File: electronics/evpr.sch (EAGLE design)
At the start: 140 parts

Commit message: Negative using signals correctly marked as negative
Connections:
- net USING_ENG renamed !USING_ENG
- new net !USING_BAT: U.ESP1.IO4
- net USING_BAT: no longer U.ESP1.IO4
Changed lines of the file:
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@@
 </segment>
 </net>
-<net name="USING_ENG" class="0">
+<net name="!USING_ENG" class="0">
 <segment>
 <pinref part="U.YY1" gate="A" pin="!ONST2"/>
@@
 <wire x1="-38.1" y1="-15.24" x2="-38.1" y2="-30.48" width="0.1524" layer="91"/>
 <wire x1="-38.1" y1="-30.48" x2="-35.56" y2="-30.48" width="0.1524" layer="91"/>
-</segment>
-<segment>
-<label x="114.3" y="152.4" size="1.778" layer="95" xref="yes"/>
-<pinref part="U.ESP1" gate="G$1" pin="IO4"/>
-<wire x1="73.66" y1="139.7" x2="96.52" y2="139.7" width="0.1524" layer="91"/>
-<wire x1="96.52" y1="139.7" x2="96.52" y2="152.4" width="0.1524" layer="91"/>
-<wire x1="96.52" y1="152.4" x2="114.3" y2="152.4" width="0.1524" layer="91"/>
 </segment>
 </net>
@@
 </segment>
 </net>
+<net name="!USING_BAT" class="0">
+<segment>
+<label x="114.3" y="152.4" size="1.778" layer="95" xref="yes"/>
+<pinref part="U.ESP1" gate="G$1" pin="IO4"/>
+<wire x1="73.66" y1="139.7" x2="96.52" y2="139.7" width="0.1524" layer="91"/>
+<wire x1="96.52" y1="139.7" x2="96.52" y2="152.4" width="0.1524" layer="91"/>
+<wire x1="96.52" y1="152.4" x2="114.3" y2="152.4" width="0.1524" layer="91"/>
+</segment>
+</net>

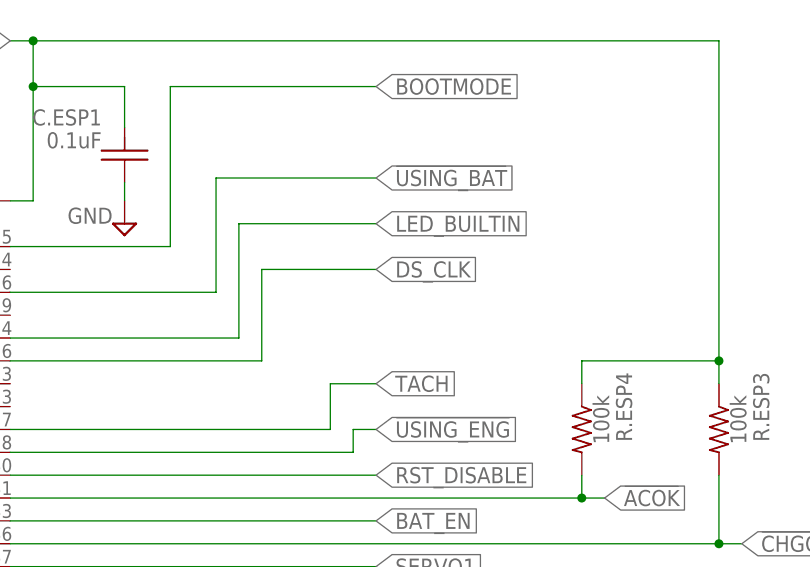
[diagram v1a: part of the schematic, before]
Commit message: Unswap DS_CLK and LED_Builtin
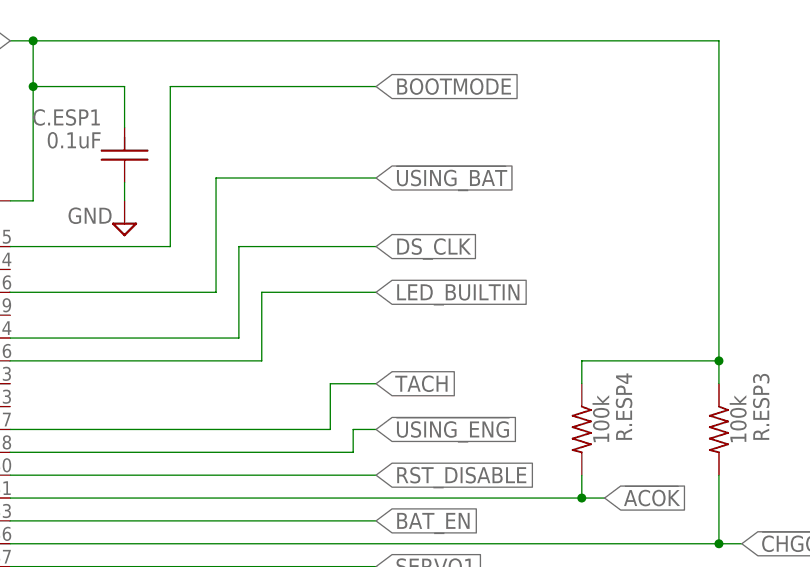
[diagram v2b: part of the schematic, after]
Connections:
- net DS_CLK: now also U.ESP1.IO12; no longer U.ESP1.IO13
- net LED_BUILTIN: now also U.ESP1.IO13; no longer U.ESP1.IO12
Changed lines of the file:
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@@
 </segment>
 <segment>
-<label x="114.3" y="142.24" size="1.778" layer="95" xref="yes"/>
-<wire x1="101.6" y1="142.24" x2="114.3" y2="142.24" width="0.1524" layer="91"/>
-<pinref part="U.ESP1" gate="G$1" pin="IO13"/>
-<wire x1="73.66" y1="132.08" x2="101.6" y2="132.08" width="0.1524" layer="91"/>
-<wire x1="101.6" y1="132.08" x2="101.6" y2="142.24" width="0.1524" layer="91"/>
+<label x="114.3" y="144.78" size="1.778" layer="95" xref="yes"/>
+<wire x1="99.06" y1="144.78" x2="114.3" y2="144.78" width="0.1524" layer="91"/>
+<pinref part="U.ESP1" gate="G$1" pin="IO12"/>
+<wire x1="99.06" y1="134.62" x2="99.06" y2="144.78" width="0.1524" layer="91"/>
+<wire x1="73.66" y1="134.62" x2="99.06" y2="134.62" width="0.1524" layer="91"/>
 </segment>
 </net>
@@
 <net name="LED_BUILTIN" class="0">
 <segment>
-<pinref part="U.ESP1" gate="G$1" pin="IO12"/>
-<wire x1="73.66" y1="134.62" x2="99.06" y2="134.62" width="0.1524" layer="91"/>
-<wire x1="99.06" y1="134.62" x2="99.06" y2="147.32" width="0.1524" layer="91"/>
-<wire x1="99.06" y1="147.32" x2="114.3" y2="147.32" width="0.1524" layer="91"/>
-<label x="114.3" y="147.32" size="1.778" layer="95" xref="yes"/>
-</segment>
-<segment>
+<wire x1="101.6" y1="132.08" x2="101.6" y2="139.7" width="0.1524" layer="91"/>
+<wire x1="101.6" y1="139.7" x2="114.3" y2="139.7" width="0.1524" layer="91"/>
+<label x="114.3" y="139.7" size="1.778" layer="95" xref="yes"/>
+<pinref part="U.ESP1" gate="G$1" pin="IO13"/>
+<wire x1="73.66" y1="132.08" x2="101.6" y2="132.08" width="0.1524" layer="91"/>
+</segment>
+<segment>

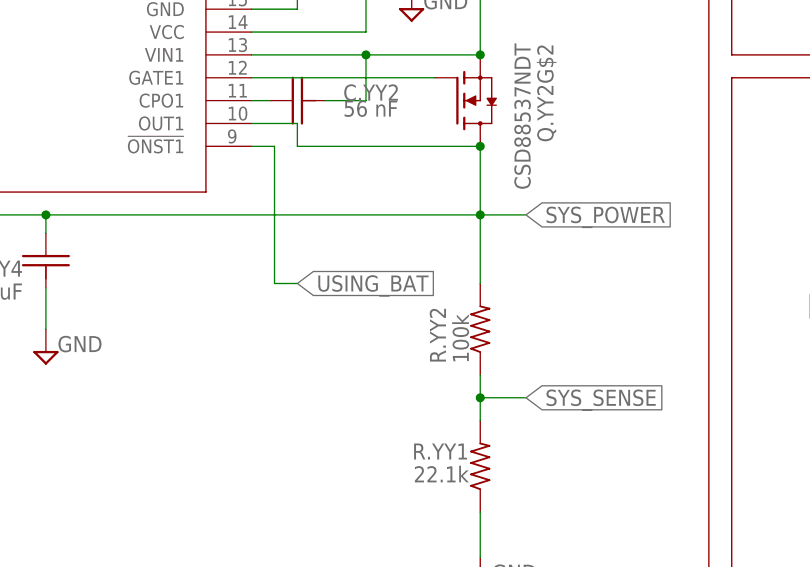
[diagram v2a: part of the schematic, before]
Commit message: Performed DRC checks, fixed minor issues, redid OSH version
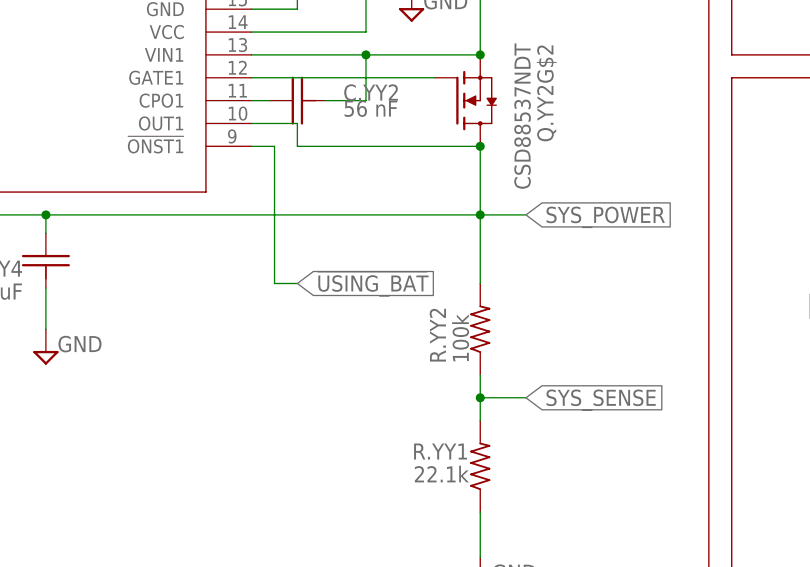
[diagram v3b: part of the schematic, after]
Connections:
- removed net USING_BAT: U.YY1.!ONST1
- net !USING_BAT: now also U.YY1.!ONST1
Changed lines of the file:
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@@
-</segment>
-</net>
-<net name="USING_BAT" class="0">
-<segment>
-<pinref part="U.YY1" gate="A" pin="!ONST1"/>
-<label x="-35.56" y="-30.48" size="1.778" layer="95" rot="MR180" xref="yes"/>
-<wire x1="-40.64" y1="-15.24" x2="-38.1" y2="-15.24" width="0.1524" layer="91"/>
-<wire x1="-38.1" y1="-15.24" x2="-38.1" y2="-30.48" width="0.1524" layer="91"/>
-<wire x1="-38.1" y1="-30.48" x2="-35.56" y2="-30.48" width="0.1524" layer="91"/>
 </segment>
 </net>
@@
 <wire x1="96.52" y1="152.4" x2="114.3" y2="152.4" width="0.1524" layer="91"/>
 </segment>
+<segment>
+<pinref part="U.YY1" gate="A" pin="!ONST1"/>
+<label x="-35.56" y="-30.48" size="1.778" layer="95" rot="MR180" xref="yes"/>
+<wire x1="-40.64" y1="-15.24" x2="-38.1" y2="-15.24" width="0.1524" layer="91"/>
+<wire x1="-38.1" y1="-15.24" x2="-38.1" y2="-30.48" width="0.1524" layer="91"/>
+<wire x1="-38.1" y1="-30.48" x2="-35.56" y2="-30.48" width="0.1524" layer="91"/>
+</segment>
 </net>
 </nets>
 </sheet>
 </sheets>
+<errors>
+</errors>
 </schematic>
 </drawing>

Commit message: Remove USB interface from EVPR, design external programmer board
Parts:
- removed C.USB1, C.USB4: 4.7uF, mccloud:C0603
- removed C.USB2, C.USB3: 0.1uF, mccloud:C0603
- removed C.USB5: 4.7 nF, mccloud:C0603
- removed Q.ESP1: DMN5L06K-7, mccloud:DMN5L06K-7
- removed Q.USB1, Q.USB2: MMBT2222A, transistor-neu-to92:MMBT2222ALT1-NPN-SOT23-BEC
- removed R.ESP1, R.USB2, R.USB3: 10k, mccloud:R0603
- removed R.USB1: 1k, mccloud:R0603
- removed R.USB5: 22.1k, mccloud:R0603
- removed R.USB6: 47.5K, mccloud:R0603
- removed R.USB7: 1M, mccloud:R0603
- removed SJ.ESP1: (no value), jumper:SJ
- removed TP11, TP14, TP15, TP3, TP5, TP7, TP8: PTR1TP10R, testpad:PTR1TP10R
- removed U.USB1: CP2102N-A02-GQFN24R, mccloud:CP2102N-A02-GQFN24R
- removed X.ESP2: RSTBTN, mccloud:RSTBTN
- removed X.USB1: 10118193-0001LF, mccloud:10118193-0001LF
- added SV1: (no value), con-lstb:MA04-2
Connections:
- removed net N$1: Q.ESP1.D, X.ESP2.1
- removed net N$16: R.USB1.1, U.USB1.RSTB
- removed net N$18: Q.USB1.E, R.USB3.2, TP14.TP, U.USB1.RTS
- removed net N$19: Q.USB2.E, R.USB2.2, TP8.TP, U.USB1.DTR
- removed net N$20: Q.USB1.B, R.USB2.1
- removed net N$21: Q.USB2.B, R.USB3.1
- removed net N$34: C.USB5.2, R.USB7.2, TP15.TP, X.USB1.SHIELD
- removed net N$39: R.USB1.2, U.USB1.VIO
- removed net N$40: C.USB1.2, C.USB2.2, TP3.TP, U.USB1.VDD
- removed net RST_DISABLE: Q.ESP1.G, R.ESP1.2, U.ESP1.IO18
- removed net USBD+: U.USB1.D+, X.USB1.D+
- removed net USBD-: U.USB1.D-, X.USB1.D-
- removed net USBSENSE: R.USB5.1, R.USB6.2, U.ESP1.IO20, U.USB1.VBUS
- removed net VUSB: C.USB3.2, C.USB4.2, Q.DS1.A, Q.ZZ2.A, R.USB5.2, TP7.TP, U.USB1.VREGIN, X.USB1.VUSB
- new net VPROG: Q.DS1.A, Q.ZZ2.A, SV1.6
- net BOOTMODE: now also SV1.3; no longer Q.USB2.C, TP11.TP
- net ESP_POWER: now also SV1.8; no longer R.ESP1.1
- net ESP_RX: now also SV1.5; no longer U.USB1.TXD
- net ESP_TX: now also SV1.7; no longer U.USB1.RXD
- net GND: now also SV1.2; no longer C.USB1.1, C.USB2.1, C.USB3.1, C.USB4.1, C.USB5.1, Q.ESP1.S, R.USB6.1, R.USB7.1, SJ.ESP1.1, U.USB1.GND, X.USB1.GND
- net RESET: now also SV1.1; no longer Q.USB1.C, SJ.ESP1.2, TP5.TP, X.ESP2.2
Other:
- note added: "ESP: ESP32 GPIO & Prog Interface"
- note removed: "ESP: ESP32 GPIO & Reset"
- note removed: "NOTE: LED_BUILTIN will blink during flashing. This is why the LED circuit is included here, rather than in the ESP32 block."
- note removed: "USB: USB Interface"
- moved on the sheet: D.USB1, R.ESP2, R.USB4

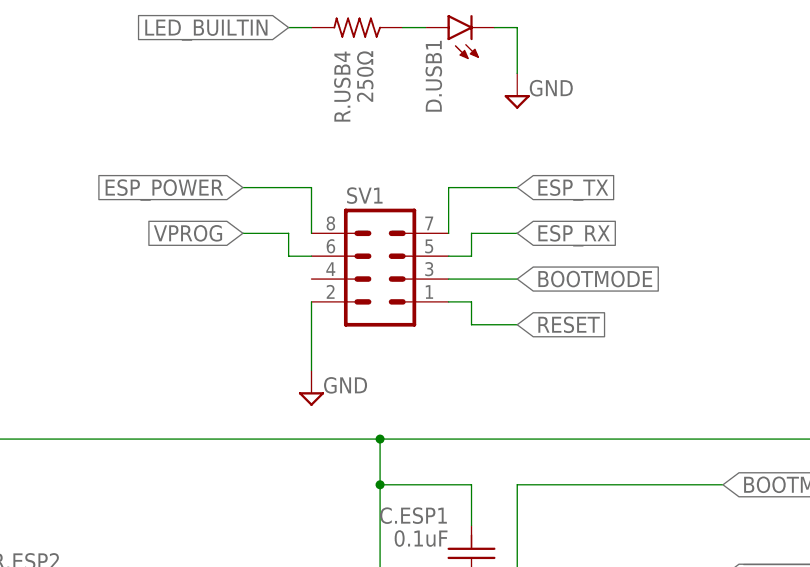
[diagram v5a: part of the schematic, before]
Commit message: Update mainboard and progboard to use smaller connector
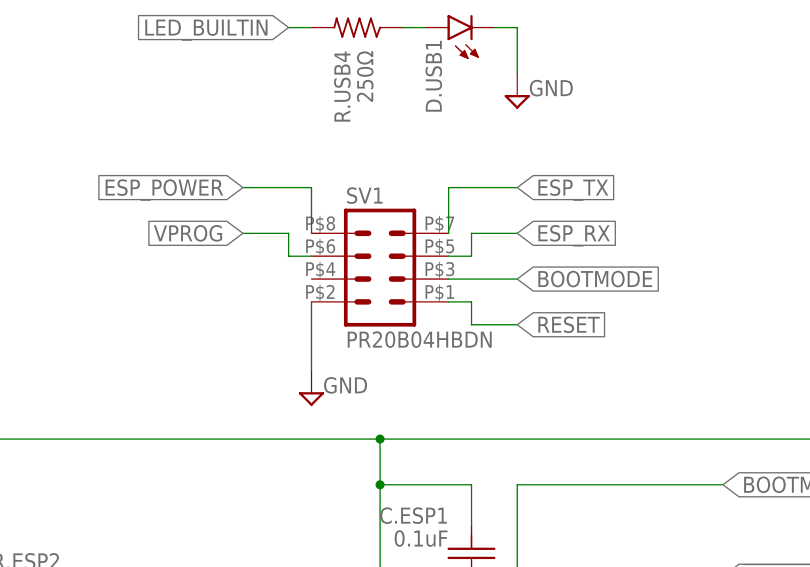
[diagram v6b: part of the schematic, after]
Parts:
- SV1: value (none) -> PR20B04HBDN; device con-lstb:MA04-2 -> mccloud:PR20B04HBDN
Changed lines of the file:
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@@
 </part>
 <part name="SUPPLY12" library="supply2" library_urn="urn:adsk.eagle:library:372" deviceset="GND" device=""/>
-<part name="SV1" library="con-lstb" library_urn="urn:adsk.eagle:library:162" deviceset="MA04-2" device="" package3d_urn="urn:adsk.eagle:package:8368/1"/>
+<part name="SV1" library="mccloud" deviceset="PR20B04HBDN" device=""/>
 <part name="SUPPLY13" library="supply2" library_urn="urn:adsk.eagle:library:372" deviceset="GND" device=""/>
 </parts>

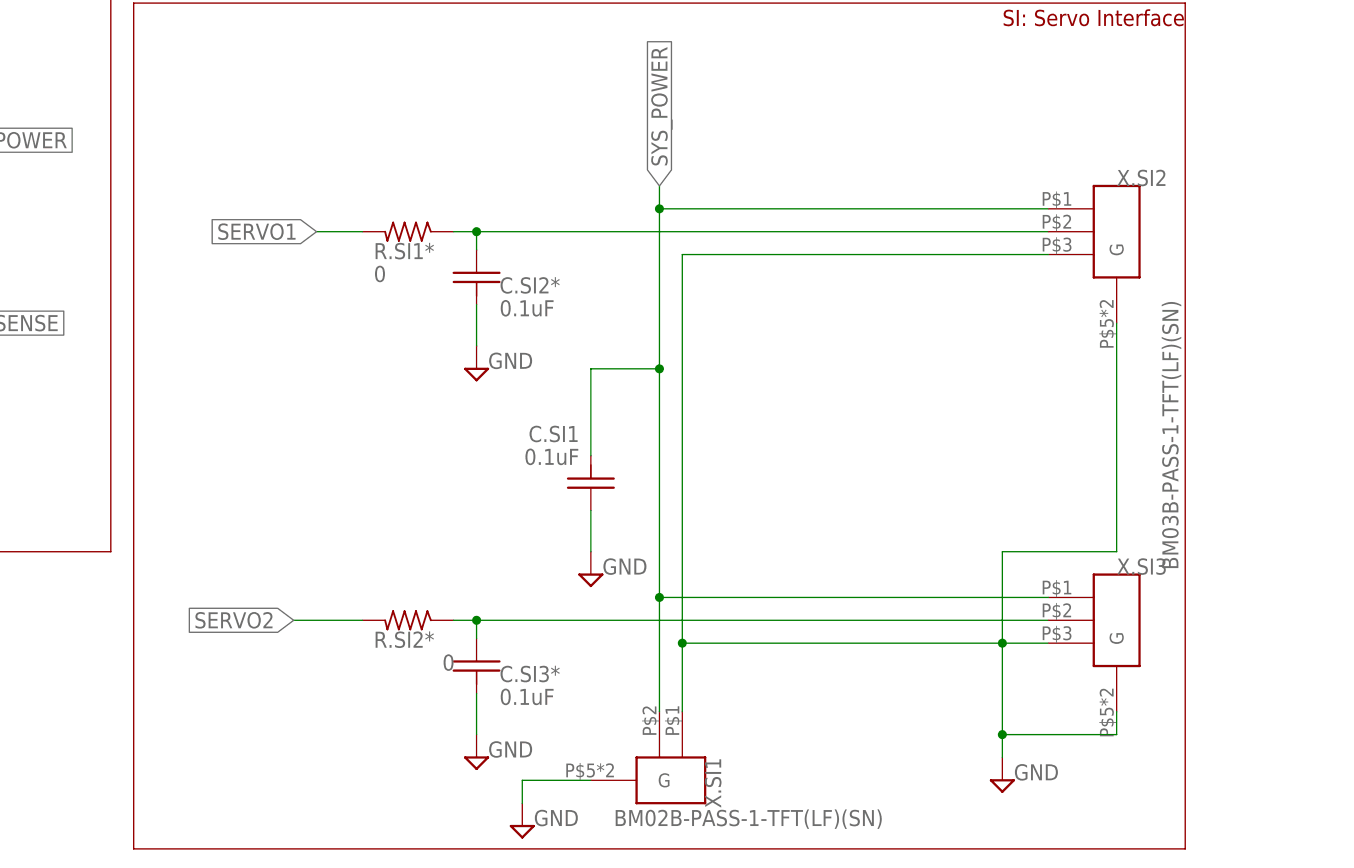
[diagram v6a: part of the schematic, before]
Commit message: Various connector changes and other miscellany
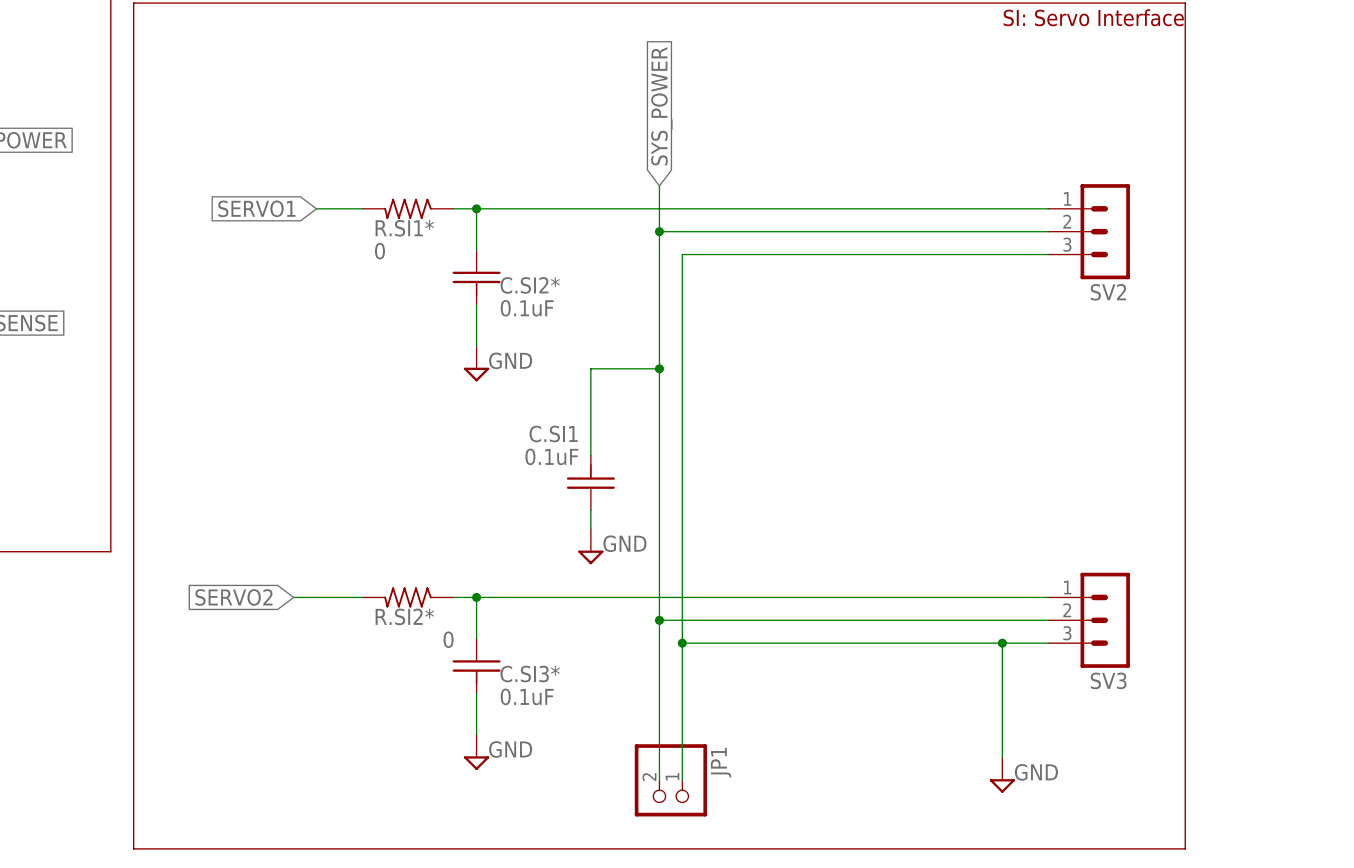
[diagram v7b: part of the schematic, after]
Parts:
- removed X.SI1: BM02B-PASS-1-TFT(LF)(SN), mccloud:BM02B-PASS-1-TFT(LF)(SN)
- removed X.SI2, X.SI3: BM03B-PASS-1-TFT(LF)(SN), mccloud:BM03B-PASS-1-TFT(LF)(SN)
- added JP1: (no value), pinhead:PINHD-1X2
- added SV2, SV3: (no value), con-lstb:MA03-1
- C.DS7, C.ZZ2: COMPONENT GRM188R61A106KE69D -> GRM188R61E106MA73J
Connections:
- net GND: now also JP1.1, SV2.3, SV3.3; no longer X.SI1.1, X.SI1.G, X.SI2.3, X.SI2.G, X.SI3.3, X.SI3.G
- net N$11: now also SV2.1; no longer X.SI2.2
- net N$12: now also SV3.1; no longer X.SI3.2
- net SYS_POWER: now also JP1.2, SV2.2, SV3.2; no longer X.SI1.2, X.SI2.1, X.SI3.1
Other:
- moved on the sheet: R.SI1*, R.SI2*

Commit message: Silkscreen adjustments, some DRC issues adjustments
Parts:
- X.BI1, X.BI2: device B2P-VH_LF__SN_:B2P-VH(LF)(SN) -> mccloud:B2P-VH(LF)(SN)
- X.VI1: device B3P-VH_LF__SN_:B3P-VH(LF)(SN) -> mccloud:B3P-VH(LF)(SN)
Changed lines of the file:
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@@
 </classes>
 <parts>
-<part name="X.VI1" library="B3P-VH_LF__SN_" deviceset="B3P-VH(LF)(SN)" device="">
+<part name="X.VI1" library="mccloud" deviceset="B3P-VH(LF)(SN)" device="">
 <attribute name="COMPONENT" value="B3P-VH(LF)(SN)"/>
 </part>
@@
 <attribute name="COMPONENT" value="RMCF0603FT100K"/>
 </part>
-<part name="X.BI1" library="B2P-VH_LF__SN_" deviceset="B2P-VH(LF)(SN)" device="">
+<part name="X.BI1" library="mccloud" deviceset="B2P-VH(LF)(SN)" device="">
 <attribute name="COMPONENT" value="B2P-VH(LF)(SN)"/>
 </part>
-<part name="X.BI2" library="B2P-VH_LF__SN_" deviceset="B2P-VH(LF)(SN)" device="">
+<part name="X.BI2" library="mccloud" deviceset="B2P-VH(LF)(SN)" device="">
 <attribute name="COMPONENT" value="B2P-VH(LF)(SN)"/>
 </part>
